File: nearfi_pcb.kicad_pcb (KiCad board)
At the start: 2 copper layers, 45.6 x 45.6 mm, 24 parts, among them J1 PWR_CONN, J2 CONN_PROG, Q1 MMBT3904, SW1 RESET, SW2 BOOT, U1 ESP32-S2-WROVER, U2 TLV1117-33

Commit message: Edited some details
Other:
- board text added: "Name: NearFi Author: Mauricio Barroso Date: 17/05/21 Version: 1.0.0 Rev: 2"
- board text removed: "Name: NearFi Author: Mauricio Barroso Date: 17/05/21 Version: 1.0 Rev: 2"

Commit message: Changed components and corrected errors
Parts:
- removed C7: 10u, Capacitor_Tantalum_SMD:CP_EIA-2012-15_AVX-P_Pad1.30x1.05mm_HandSolder
- removed J2: CONN_PROG, Connector_PinHeader_2.54mm:PinHeader_1x04_P2.54mm_Vertical
- removed the R4 at (163.3, 50.3)
- removed SW2: BOOT, Button_Switch_SMD:SW_SPST_TL3342
- added C5: 10u, Capacitor_Tantalum_SMD:CP_EIA-2012-15_AVX-P_Pad1.30x1.05mm_HandSolder, F.Cu at (142.0, 77.0)
- added J3: CONN_PROG, Connector_PinHeader_2.54mm:PinHeader_2x03_P2.54mm_Vertical, F.Cu at (161.8, 55.1)
- added R2: 10K, Resistor_SMD:R_0805_2012Metric_Pad1.20x1.40mm_HandSolder, F.Cu at (163.3, 50.3)
- BZ1: footprint Buzzer_Beeper:Buzzer_Murata_PKMCS0909E4000-R1 -> Buzzer_Beeper:Buzzer_12x9.5RM7.6
- D1: value NeoPixel_THT -> WS2812B; footprint LED_THT:LED_D5.0mm-4_RGB -> LED_SMD:LED_WS2812B_PLCC4_5.0x5.0mm_P3.2mm
- SW1: value RESET -> FUNCTION; footprint Button_Switch_SMD:SW_SPST_TL3342 -> Button_Switch_THT:SW_Tactile_SPST_Angled_PTS645Vx31-2LFS
- moved SW1 26.7 mm to (161.3, 82.5)
- moved C1 7.89 mm to (163.1, 70.9), turned to 0 degrees
- moved D1 6.57 mm to (163.1, 66.0), turned to 90 degrees
- moved Q1 4.06 mm to (130.8, 56.9)
- moved R1 4.06 mm to (136.1, 56.9)
- moved BZ1 3.87 mm to (136.9, 66.0), turned to 180 degrees
- renumbered C5 to C2, C6 to C3, C10 to C6, R2 to R1, R1 to R4
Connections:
- C4 pad 2: Net-(C4-Pad2) -> /RESET
- D1 pad 1: (no net) -> +3V3
- D1 pad 2: GND -> (no net)
- D1 pad 3: +3V3 -> GND
- SW1 pad 2: Net-(C4-Pad2) -> /FUNC
- U1 pad 11: /BUZZER -> (no net)
- U1 pad 27: (no net) -> /FUNC
- U1 pad 3: Net-(SW2-Pad2) -> /BOOT
- U1 pad 32: (no net) -> /RGB
- U1 pad 39: /RGB -> (no net)
- U1 pad 41: Net-(C4-Pad2) -> /RESET
- U1 pad 7: (no net) -> /BUZZER
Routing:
- net /BOOT: track 0.00 -> 28.0 mm
- net Net-(C4-Pad2): track 20.8 -> 0.00 mm
- net /RXD: track 21.5 -> 6.15 mm
- net Net-(SW2-Pad2): track 13.0 -> 0.00 mm
- net /RESET: track 0.00 -> 12.8 mm
- net /FUNC: track 0.00 -> 12.5 mm
- net /RGB: track 15.2 -> 3.73 mm
- net /TXD: track 17.9 -> 7.10 mm
- net +3V3: track 102.4 -> 95.8 mm, vias 15 -> 14
- net Net-(BZ1-Pad2): track 10.8 -> 8.77 mm
- net /BUZZER: track 5.14 -> 3.59 mm
- net GND: track 4.49 -> 3.36 mm, vias 66 -> 65
- net (no net): vias 0 -> 1
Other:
- board text added: "Name: NearFi Author: Mauricio Barroso Date: 29/07/21 Version: 1.1 Rev: 3"
- board text removed: "Name: NearFi Author: Mauricio Barroso Date: 17/05/21 Version: 1.0.0 Rev: 2"

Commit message: Updated PCB
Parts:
- removed U1: ESP32-S2-WROVER, RF_Module:ESP32-S2-WROVER
- added U3: ESP32-S2-WROOM, Espressif:ESP32-S2-WROOM, F.Cu at (149.4, 59.0)
- C5: footprint Capacitor_Tantalum_SMD:CP_EIA-2012-15_AVX-P_Pad1.30x1.05mm_HandSolder -> Capacitor_Tantalum_SMD:CP_EIA-3216-18_Kemet-A_Pad1.58x1.35mm_HandSolder
- C6: value 10u -> 100u; footprint Capacitor_Tantalum_SMD:CP_EIA-2012-15_AVX-P_Pad1.30x1.05mm_HandSolder -> Capacitor_Tantalum_SMD:CP_EIA-3528-21_Kemet-B_Pad1.50x2.35mm_HandSolder
- moved R3 5.14 mm to (147.6, 73.7)
- moved R4 4.38 mm to (141.7, 73.7)
- moved D2 2.90 mm to (136.1, 73.7)
- moved C6 1.85 mm to (136.1, 76.5), turned to 180 degrees
- moved C5 0.57 mm to (141.7, 76.5)
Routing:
- net +3V3: track 95.8 -> 89.2 mm, vias 14 -> 17
- net Net-(R3-Pad1): track 8.20 -> 2.57 mm
- net Net-(D2-Pad2): track 2.10 -> 3.63 mm
- net /FUNC: track 12.5 -> 13.9 mm
- net +5V: track 9.29 -> 9.80 mm, vias 3 -> 5
- net GND: vias 65 -> 57
- net (no net): vias 1 -> 0
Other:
- board text added: "Name: NearFi Author: Mauricio Barroso Date: 16/10/21 Version: 1.2 Rev: 4"
- board text removed: "Name: NearFi Author: Mauricio Barroso Date: 29/07/21 Version: 1.1 Rev: 3"

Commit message: improved schematic and pcb layout, finished rev D
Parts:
- removed J3: CONN_PROG, Connector_PinHeader_2.54mm:PinHeader_2x03_P2.54mm_Vertical
- added C10: 100n, Capacitor_SMD:C_0603_1608Metric, F.Cu at (170.2, 63.0)
- added C11: 100n, Capacitor_SMD:C_0603_1608Metric, F.Cu at (170.2, 57.7)
- added C12: 100n, Capacitor_SMD:C_0603_1608Metric, F.Cu at (159.0, 81.3)
- added C7: 100n, Capacitor_SMD:C_0603_1608Metric, F.Cu at (154.2, 65.0)
- added D3: 1N4148WS, Diode_SMD:D_SOD-323, F.Cu at (161.0, 68.3)
- added D4: WS2812B-2020, Misc:WS2812B-2020, F.Cu at (154.2, 63.0)
- added D5: ESD9B5.0ST5G, Diode_SMD:D_SOD-923, F.Cu at (158.5, 80.0)
- added D6: RED_LED, LED_SMD:LED_0603_1608Metric, F.Cu at (169.4, 69.1)
- added D8: ESD9B5.0ST5G, Diode_SMD:D_SOD-923, F.Cu at (163.8, 63.8)
- added D9: ESD9B5.0ST5G, Diode_SMD:D_SOD-923, F.Cu at (163.8, 62.2)
- added G***: LOGO, Misc:Getbit_Logo, F.Cu at (149.4, 70.1)
- added J2: PROG_CNN, Connector_PinHeader_1.27mm:PinHeader_2x03_P1.27mm_Vertical_SMD, F.Cu at (167.1, 51.3)
- added R10: 1K, Resistor_SMD:R_0603_1608Metric, F.Cu at (139.2, 55.6)
- added R5: 107K, Resistor_SMD:R_0603_1608Metric, F.Cu at (168.9, 55.1)
- added R6: 10K, Resistor_SMD:R_0603_1608Metric, F.Cu at (159.0, 78.7)
- added R7: 5.1K, Resistor_SMD:R_0603_1608Metric, F.Cu at (169.4, 67.6)
- added R8: 10K, Resistor_SMD:R_0603_1608Metric, F.Cu at (159.5, 55.1)
- added R9: 124K, Resistor_SMD:R_0603_1608Metric, F.Cu at (165.4, 55.1)
- added TP1: SDA, TestPoint:TestPoint_Pad_D1.0mm, F.Cu at (160.7, 63.9)
- added TP2: SCL, TestPoint:TestPoint_Pad_D1.0mm, F.Cu at (160.7, 61.8)
- added TP3: +5V, TestPoint:TestPoint_Pad_D1.0mm, F.Cu at (142.6, 78.4)
- added TP4: +3V3, TestPoint:TestPoint_Pad_D1.0mm, F.Cu at (164.6, 65.7)
- added U4: TPL5010, Package_TO_SOT_SMD:SOT-23-6, F.Cu at (167.1, 57.7)
- added U5: ESP32-S3-MINI-1, Espressif:ESP32-S3-MINI-1, F.Cu at (149.4, 53.4)
- added kibuzzard-64889FDD: G***, kibuzzard-64889FDD, F.Cu at (140.3, 78.4)
- added kibuzzard-6488A00A: G***, kibuzzard-6488A00A, F.Cu at (158.6, 61.8)
- added kibuzzard-6488A011: G***, kibuzzard-6488A011, F.Cu at (158.6, 63.9)
- added kibuzzard-6488A021: G***, kibuzzard-6488A021, F.Cu at (162.3, 65.7)
- BZ1: value Buzzer -> PKMCS0909E; footprint Buzzer_Beeper:Buzzer_12x9.5RM7.6 -> Buzzer_Beeper:Buzzer_Murata_PKMCS0909E
- C1: value 100n -> 1u; footprint Capacitor_SMD:C_0805_2012Metric_Pad1.18x1.45mm_HandSolder -> Capacitor_SMD:C_0603_1608Metric
- C2, C3: footprint Capacitor_SMD:C_0805_2012Metric_Pad1.18x1.45mm_HandSolder -> Capacitor_SMD:C_0603_1608Metric
- C4: value 1u -> 100n; footprint Capacitor_SMD:C_0805_2012Metric_Pad1.18x1.45mm_HandSolder -> Capacitor_SMD:C_0603_1608Metric
- D1: value WS2812B -> WS2812B-2020; footprint LED_SMD:LED_WS2812B_PLCC4_5.0x5.0mm_P3.2mm -> Misc:WS2812B-2020
- D2: value LED_PWR -> 1N4148WS; footprint LED_SMD:LED_0805_2012Metric_Castellated -> Diode_SMD:D_SOD-323
- H1, H2, H3, H4: value MountingHole_Pad -> Hole
- J1: value PWR_CONN -> PWR_CNN; footprint Connector_USB:USB_Micro-B_Molex_47346-0001 -> Misc:TYPE-C-31-M-17
- R1, R3: footprint Resistor_SMD:R_0805_2012Metric_Pad1.20x1.40mm_HandSolder -> Resistor_SMD:R_0603_1608Metric
- R2: value 10K -> 1K; footprint Resistor_SMD:R_0805_2012Metric_Pad1.20x1.40mm_HandSolder -> Resistor_SMD:R_0603_1608Metric
- R4: value 5.1K -> 10K; footprint Resistor_SMD:R_0805_2012Metric_Pad1.20x1.40mm_HandSolder -> Resistor_SMD:R_0603_1608Metric
- SW1: value FUNCTION -> SRST_BTN; footprint Button_Switch_THT:SW_Tactile_SPST_Angled_PTS645Vx31-2LFS -> Button_Switch_THT:SW_Tactile_SPST_Angled_PTS645Vx39-2LFS
- U3: value ESP32-S2-WROOM -> AT24CS02-STUM; footprint Espressif:ESP32-S2-WROOM -> Package_TO_SOT_SMD:SOT-23-5
- moved D2 32.0 mm to (163.8, 57.7), turned to -90 degrees
- moved R1 31.2 mm to (167.1, 60.5)
- moved C6 29.8 mm to (164.8, 68.3)
- moved R3 28.9 mm to (160.3, 47.8), turned to 90 degrees
- moved U2 27.9 mm to (166.6, 73.7), turned to 0 degrees
- moved R4 24.6 mm to (159.5, 56.6), turned to 180 degrees
- moved R2 24.1 mm to (139.2, 50.0), turned to 0 degrees
- moved C1 23.5 mm to (158.8, 47.8), turned to 90 degrees
- moved C4 21.5 mm to (140.0, 47.8)
- moved C5 19.5 mm to (161.0, 73.7), turned to 90 degrees
- moved D1 18.8 mm to (144.5, 63.0), turned to 0 degrees
- moved U3 18.2 mm to (167.1, 63.0)
- moved C3 16.4 mm to (144.5, 65.0), turned to 180 degrees
- moved Q1 9.32 mm to (139.2, 52.8)
- moved C2 3.97 mm to (138.4, 47.8)
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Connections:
- BZ1 pad 1: +3V3 -> +5V
- C1 pad 1: +3V3 -> GND
- C1 pad 2: GND -> /HRST_I
- C2 pad 1: GND -> +3.3V
- C2 pad 2: +3V3 -> GND
- C3 pad 2: +3V3 -> +3.3V
- C4 pad 1: GND -> +3.3V
- C4 pad 2: /RESET -> GND
- C6 pad 1: +3V3 -> +3.3V
- D1 pad 1: +3V3 -> Net-(D1-Pad1)
- D1 pad 2: (no net) -> GND
- D1 pad 3: GND -> /WS2812B_S
- D1 pad 4: /RGB -> +3.3V
- D2 pad 1: GND -> /HRST_I
- R1 pad 1: /BUZZER -> Net-(R1-Pad1)
- R1 pad 2: Net-(Q1-Pad1) -> GND
- R2 pad 1: /RESET -> Net-(Q1-Pad1)
- R2 pad 2: +3V3 -> /BUZZER_S
- R3 pad 1: Net-(R3-Pad1) -> +3.3V
- R3 pad 2: +3V3 -> /HRST_I
- R4 pad 1: Net-(D2-Pad2) -> +3.3V
- R4 pad 2: +3V3 -> /I2C_SDA_S
- SW1 pad 2: /FUNC -> /SRST_S
- U2 pad 2: +3V3 -> +3.3V
- U3 pad 1: GND -> /I2C_SCL_S
- U3 pad 2: +3V3 -> GND
- U3 pad 3: /BOOT -> /I2C_SDA_S
- U3 pad 4: (no net) -> +3.3V
- U3 pad 5: (no net) -> Net-(R1-Pad1)
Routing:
- net +3V3: track 89.2 -> 0.00 mm, vias 17 -> 0
- net +5V: track 9.80 -> 59.9 mm
- net +3.3V: track 0.00 -> 39.7 mm, vias 0 -> 17
- net /BOOT_I: track 0.00 -> 29.9 mm, vias 0 -> 2
- net /SRST_S: track 0.00 -> 28.6 mm
- net /BOOT: track 27.7 -> 0.00 mm
- net /HRST_I: track 0.00 -> 18.1 mm, vias 0 -> 2
- net /I2C_SDA_S: track 0.00 -> 16.5 mm
- net /I2C_SCL_S: track 0.00 -> 16.2 mm
- net /FUNC: track 13.9 -> 0.00 mm
- net /RESET: track 12.7 -> 0.00 mm
- net /DONE_S: track 0.00 -> 12.5 mm
- net /WAKE_S: track 0.00 -> 12.3 mm
- net /UART_TX_O: track 0.00 -> 9.32 mm
- net /UART_RX_I: track 0.00 -> 9.21 mm, vias 0 -> 2
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- added copper zone on B.Cu, net +3.3V
- added copper zone on In1.Cu, net GND
- added copper zone on In2.Cu, net GND
- removed copper zone on B.Cu, net +3V3
- removed copper zone on F.Cu, net +3V3
- removed copper zone on F.Cu, net +5V
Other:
- outline, holes or cut-outs redrawn
- copper layers 2 -> 4
- net class Default removed
- board text added: "Designed in Bolivia Assembled in China"
- board text added: "NearFi Rev D 06/23"
- board text removed: "Name: NearFi Author: Mauricio Barroso Date: 16/10/21 Version: 1.2 Rev: 4"

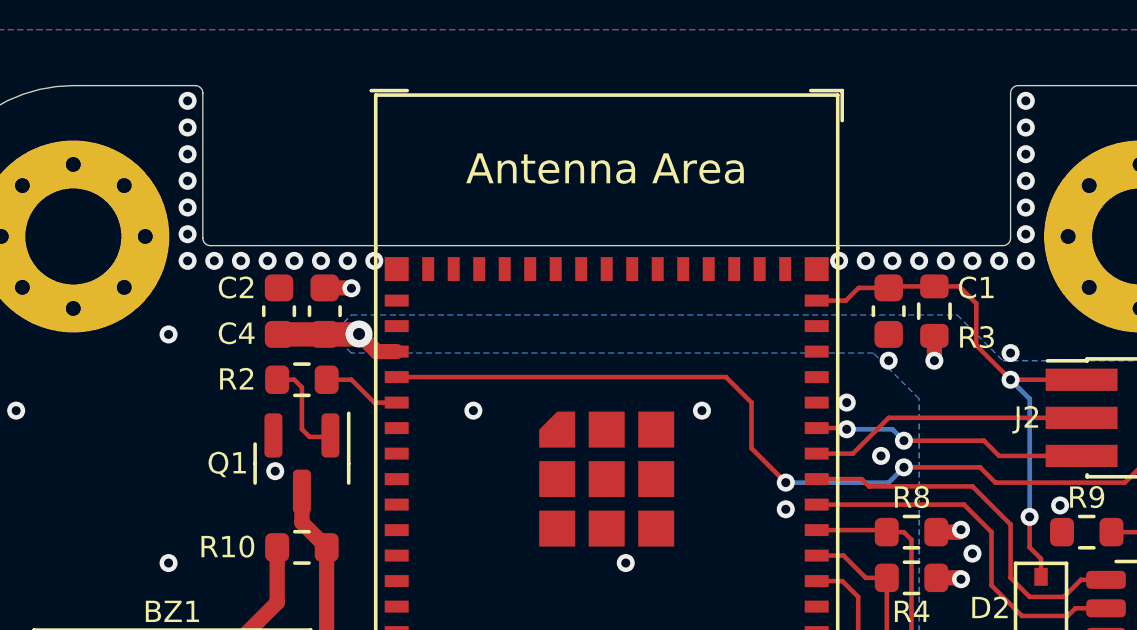
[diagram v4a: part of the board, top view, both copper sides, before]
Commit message: improved esp32s3 module +3V3 power trace
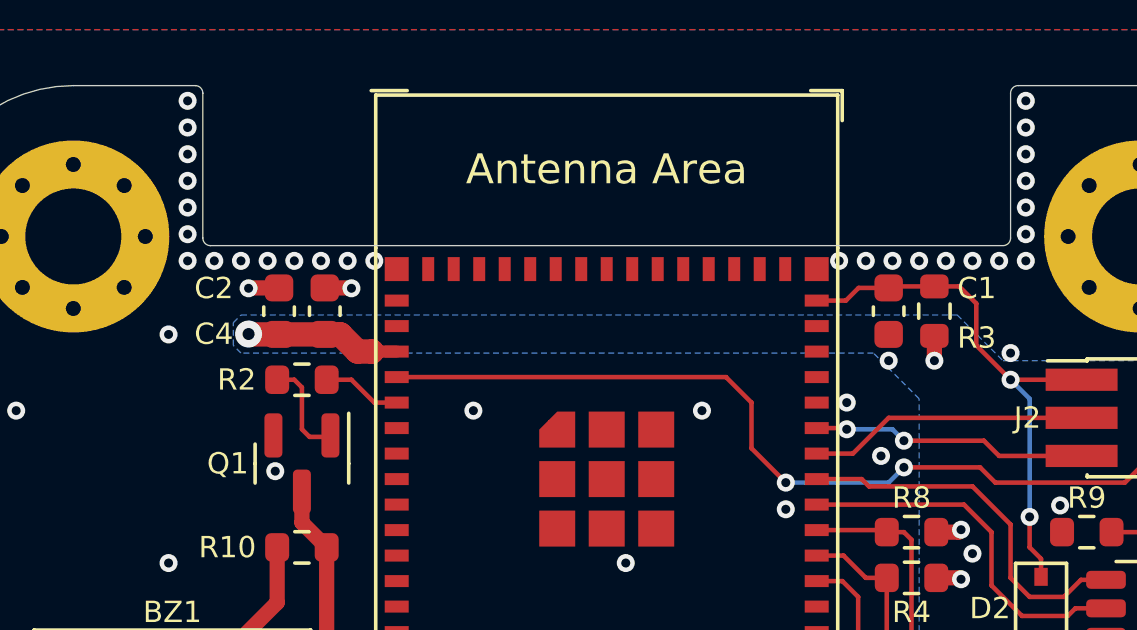
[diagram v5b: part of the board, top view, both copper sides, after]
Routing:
- net GND: track 1.79 -> 2.81 mm, vias 98 -> 99
- net +3.3V: track 39.7 -> 40.7 mm
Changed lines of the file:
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@@
     (property "Sheetname" "")
     (attr smd)
-    (fp_text reference "C2" (at 0.762 -0.762 180) (layer "F.SilkS")
+    (fp_text reference "C2" (at 0.762 -1.524 180) (layer "F.SilkS")
       (effects (font (size 0.7112 0.7112) (thickness 0.15)) (justify right))
     )
@@
     (property "Sheetname" "")
     (attr smd)
-    (fp_text reference "C4" (at -0.762 -2.286 180) (layer "F.SilkS")
+    (fp_text reference "C4" (at -0.762 -3.048 180) (layer "F.SilkS")
       (effects (font (size 0.7112 0.7112) (thickness 0.15)) (justify right))
     )
@@
     (attr board_only exclude_from_pos_files exclude_from_bom)
     (fp_text reference "kibuzzard-64889FDD" (at 0 -3.713903) (layer "F.SilkS") hide
-      (effects (font (size 0 0)))
+      (effects (font (size 0 0) (thickness 0.15)))
     )
     (fp_text value "G***" (at 0 3.713903) (layer "F.SilkS") hide
-      (effects (font (size 0 0)))
+      (effects (font (size 0 0) (thickness 0.15)))
     )
     (fp_poly (pts
@@
     (attr board_only exclude_from_pos_files exclude_from_bom)
     (fp_text reference "kibuzzard-6488A021" (at 0 -3.722793) (layer "F.SilkS") hide
-      (effects (font (size 0 0)))
+      (effects (font (size 0 0) (thickness 0.15)))
     )
     (fp_text value "G***" (at 0 3.722793) (layer "F.SilkS") hide
-      (effects (font (size 0 0)))
+      (effects (font (size 0 0) (thickness 0.15)))
     )
     (fp_poly (pts
@@
     (attr board_only exclude_from_pos_files exclude_from_bom)
     (fp_text reference "kibuzzard-6488A00A" (at 0 -3.722793) (layer "F.SilkS") hide
-      (effects (font (size 0 0)))
+      (effects (font (size 0 0) (thickness 0.15)))
     )
     (fp_text value "G***" (at 0 3.722793) (layer "F.SilkS") hide
-      (effects (font (size 0 0)))
+      (effects (font (size 0 0) (thickness 0.15)))
     )
     (fp_poly (pts
@@
     (attr board_only exclude_from_pos_files exclude_from_bom)
     (fp_text reference "kibuzzard-6488A011" (at 0 -3.722793) (layer "F.SilkS") hide
-      (effects (font (size 0 0)))
+      (effects (font (size 0 0) (thickness 0.15)))
     )
     (fp_text value "G***" (at 0 3.722793) (layer "F.SilkS") hide
-      (effects (font (size 0 0)))
+      (effects (font (size 0 0) (thickness 0.15)))
     )
     (fp_poly (pts
@@
     (effects (font (size 0.7112 0.7112) (thickness 0.1524)) (justify left))
   )
+  (segment (start 138.43 46.977) (end 137.427 46.977) (width 0.508) (layer "F.Cu") (net 1))
   (segment (start 139.954 46.977) (end 140.83 46.977) (width 0.508) (layer "F.Cu") (net 1))
   (segment (start 140.83 46.977) (end 140.843 46.99) (width 0.508) (layer "F.Cu") (net 1))
+  (segment (start 137.427 46.977) (end 137.414 46.99) (width 0.508) (layer "F.Cu") (net 1))
   (segment (start 170.18 62.217) (end 171.056 62.217) (width 0.508) (layer "F.Cu") (net 1))
   (segment (start 171.056 62.217) (end 171.069 62.23) (width 0.508) (layer "F.Cu") (net 1))
@@
   (via (at 157.353 50.8) (size 0.6) (drill 0.3) (layers "F.Cu" "B.Cu") (free) (net 1))
   (via (at 152.019 79.121) (size 0.6) (drill 0.3) (layers "F.Cu" "B.Cu") (free) (net 1))
+  (via (at 137.414 46.99) (size 0.6) (drill 0.3) (layers "F.Cu" "B.Cu") (net 1))
   (via (at 157.226 60.325) (size 0.6) (drill 0.3) (layers "F.Cu" "B.Cu") (free) (net 1))
   (via (at 155.067 79.008) (size 0.6) (drill 0.3) (layers "F.Cu" "B.Cu") (free) (net 1))
@@
   (segment (start 165.862 65.659) (end 166.37 66.167) (width 0.1524) (layer "F.Cu") (net 4))
   (segment (start 143.751 65.024) (end 143.751 65.9) (width 0.508) (layer "F.Cu") (net 4))
+  (segment (start 142.352 49.1) (end 141.527 49.1) (width 0.4064) (layer "F.Cu") (net 4))
   (segment (start 143.751 64.376) (end 143.611 64.236) (width 0.508) (layer "F.Cu") (net 4))
+  (segment (start 140.475 48.527) (end 141.0462 49.0982) (width 0.8128) (layer "F.Cu") (net 4))
+  (segment (start 138.43 48.527) (end 139.954 48.527) (width 0.8128) (layer "F.Cu") (net 4))
   (segment (start 169.774 73.66) (end 168.402 73.66) (width 0.508) (layer "F.Cu") (net 4))
   (segment (start 163.474 73.66) (end 164.846 73.66) (width 0.508) (layer "F.Cu") (net 4))
@@
   (segment (start 169.774 75.921) (end 169.799 75.946) (width 0.508) (layer "F.Cu") (net 4))
   (segment (start 170.18 58.433) (end 169.405 58.433) (width 0.508) (layer "F.Cu") (net 4))
+  (segment (start 141.5252 49.0982) (end 141.527 49.1) (width 0.8128) (layer "F.Cu") (net 4))
   (segment (start 153.403 64.376) (end 153.263 64.236) (width 0.508) (layer "F.Cu") (net 4))
   (segment (start 143.751 65.9) (end 143.764 65.913) (width 0.508) (layer "F.Cu") (net 4))
@@
   (segment (start 169.23 63.942) (end 168.2695 63.942) (width 0.508) (layer "F.Cu") (net 4))
   (segment (start 166.471 68.326) (end 166.471 66.776) (width 0.508) (layer "F.Cu") (net 4))
-  (segment (start 141.683 49.1) (end 141.097 48.514) (width 0.508) (layer "F.Cu") (net 4))
   (segment (start 153.403 65.024) (end 153.403 64.376) (width 0.508) (layer "F.Cu") (net 4))
   (segment (start 170.18 58.433) (end 171.056 58.433) (width 0.508) (layer "F.Cu") (net 4))
   (segment (start 160.337 56.642) (end 161.117 56.642) (width 0.508) (layer "F.Cu") (net 4))
   (segment (start 169.23 58.608) (end 168.2695 58.608) (width 0.508) (layer "F.Cu") (net 4))
-  (segment (start 138.43 48.527) (end 139.954 48.527) (width 0.8128) (layer "F.Cu") (net 4))
   (segment (start 168.593 66.739) (end 168.529 66.675) (width 0.508) (layer "F.Cu") (net 4))
   (segment (start 160.337 55.118) (end 161.082 55.118) (width 0.508) (layer "F.Cu") (net 4))
   (segment (start 153.403 65.9) (end 153.416 65.913) (width 0.508) (layer "F.Cu") (net 4))
+  (segment (start 138.43 48.527) (end 137.427 48.527) (width 0.8128) (layer "F.Cu") (net 4))
   (segment (start 161.117 56.642) (end 161.163 56.688) (width 0.508) (layer "F.Cu") (net 4))
   (segment (start 164.592 65.659) (end 165.862 65.659) (width 0.1524) (layer "F.Cu") (net 4))
-  (segment (start 141.084 48.527) (end 141.097 48.514) (width 0.8128) (layer "F.Cu") (net 4))
   (segment (start 153.403 65.024) (end 153.403 65.9) (width 0.508) (layer "F.Cu") (net 4))
+  (segment (start 137.427 48.527) (end 137.414 48.514) (width 0.8128) (layer "F.Cu") (net 4))
+  (segment (start 139.954 48.527) (end 140.475 48.527) (width 0.8128) (layer "F.Cu") (net 4))
   (segment (start 168.593 67.564) (end 168.593 66.739) (width 0.508) (layer "F.Cu") (net 4))
   (segment (start 170.18 63.767) (end 171.056 63.767) (width 0.508) (layer "F.Cu") (net 4))
@@
   (segment (start 160.274 48.577) (end 160.274 49.403) (width 0.508) (layer "F.Cu") (net 4))
   (segment (start 171.056 58.433) (end 171.069 58.42) (width 0.508) (layer "F.Cu") (net 4))
-  (segment (start 142.352 49.1) (end 141.683 49.1) (width 0.508) (layer "F.Cu") (net 4))
   (segment (start 171.056 63.767) (end 171.069 63.754) (width 0.508) (layer "F.Cu") (net 4))
-  (segment (start 139.954 48.527) (end 141.084 48.527) (width 0.8128) (layer "F.Cu") (net 4))
+  (segment (start 141.0462 49.0982) (end 141.5252 49.0982) (width 0.8128) (layer "F.Cu") (net 4))
   (segment (start 143.751 65.024) (end 143.751 64.376) (width 0.508) (layer "F.Cu") (net 4))
   (segment (start 169.082 50.038) (end 170.688 50.038) (width 0.508) (layer "F.Cu") (net 4))
@@
   (via (at 160.274 49.403) (size 0.6) (drill 0.3) (layers "F.Cu" "B.Cu") (net 4))
   (via (at 161.036 66.675) (size 0.6) (drill 0.3) (layers "F.Cu" "B.Cu") (net 4))
-  (via (at 141.097 48.514) (size 0.9) (drill 0.4) (layers "F.Cu" "B.Cu") (net 4))
+  (via (at 137.414 48.514) (size 0.9) (drill 0.4) (layers "F.Cu" "B.Cu") (net 4))
   (via (at 171.069 63.754) (size 0.6) (drill 0.3) (layers "F.Cu" "B.Cu") (net 4))
   (via (at 153.416 65.913) (size 0.6) (drill 0.3) (layers "F.Cu" "B.Cu") (net 4))
@@
         (xy 159.766 50.673)
         (xy 158.242 49.149)
-        (xy 140.843 49.149)
-        (xy 140.589 48.895)
-        (xy 140.589 48.133)
-        (xy 140.843 47.879)
+        (xy 137.16 49.149)
+        (xy 136.906 48.895)
+        (xy 136.906 48.133)
+        (xy 137.16 47.879)
       )
     )

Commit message: finished rev D
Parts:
- moved TP3 4.24 mm to (146.8, 77.7)
- moved kibuzzard-64889FDD 4.24 mm to (144.5, 77.7)
- moved G*** 1.78 mm to (149.4, 68.3)
- moved C12 0.76 mm to (159.0, 80.5)
- moved D5 0.76 mm to (158.5, 79.2)
- moved R6 0.76 mm to (159.0, 78.0)
- moved SW1 0.76 mm to (161.3, 82.3)
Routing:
- net +5V: track 59.9 -> 56.6 mm
- net /SRST_S: track 28.6 -> 27.9 mm
- net GND: vias 99 -> 69
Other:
- outline, holes or cut-outs redrawn
